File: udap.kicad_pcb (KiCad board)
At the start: 2 copper layers, 25 x 10 mm, 25 parts, among them J201 Conn_02x04_Counter_Clockwise, P1 USB_C_Plug, U2 MIC5245-3.3YM5, U201 NUF6401MNT1, U202 STM32F042F6Px, U4 NUF2042XV6T1G

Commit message: Minor fix
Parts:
- moved C2 0.40 mm to (93.5, 106.0)
- moved C5 0.40 mm to (94.6, 106.0)
- moved F1 0.14 mm to (95.9, 109.4)
- moved C1 0.10 mm to (105.5, 108.3)
- moved R2 0.10 mm to (105.5, 110.1)
- moved C3 0.10 mm to (96.2, 106.9)
- moved C4 0.10 mm to (105.5, 107.4)
- moved R201 0.10 mm to (105.5, 109.2)
- moved R202 0.10 mm to (105.5, 106.5)
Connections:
- net /bmp_core/BOOT0 renamed /core/BOOT0
- net /bmp_core/DM_P renamed /core/DM_P
- net /bmp_core/DP_P renamed /core/DP_P
- net /bmp_core/LED0 renamed /core/LED0
- net /bmp_core/LED1 renamed /core/LED1
- net /bmp_core/NRST renamed /core/NRST
- net /bmp_core/SWCLK renamed /core/SWCLK
- net /bmp_core/SWDIO renamed /core/SWDIO
- net /bmp_core/TGT_RST renamed /core/TGT_RST
- net /bmp_core/TGT_RX renamed /core/TGT_RX
- net /bmp_core/TGT_SWCLK renamed /core/TGT_SWCLK
- net /bmp_core/TGT_SWCLKo renamed /core/TGT_SWCLKo
- net /bmp_core/TGT_SWDIO renamed /core/TGT_SWDIO
- net /bmp_core/TGT_SWDIOo renamed /core/TGT_SWDIOo
- net /bmp_core/TGT_SWO renamed /core/TGT_SWO
- net /bmp_core/TGT_SWOo renamed /core/TGT_SWOo
- net /bmp_core/TGT_TX renamed /core/TGT_TX
- J201 pad 2: /bmp_core/TGT_RSTo -> /core/TGT_RXo
- J201 pad 3: /bmp_core/TGT_RXo -> /core/TGT_TXo
- J201 pad 4: /bmp_core/TGT_TXo -> GND
- J201 pad 8: GND -> /core/TGT_RSTo
- U201 pad 10: /bmp_core/TGT_RSTo -> /core/TGT_RSTo
- U201 pad 7: /bmp_core/TGT_RXo -> /core/TGT_RXo
- U201 pad 8: /bmp_core/TGT_TXo -> /core/TGT_TXo
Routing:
- net /bmp_core/TGT_RSTo: track 7.58 -> 0.00 mm, vias 2 -> 0
- net /core/TGT_RSTo: track 0.00 -> 7.10 mm, vias 0 -> 1
- net /bmp_core/TGT_TXo: track 6.34 -> 0.00 mm
- net /core/TGT_RXo: track 0.00 -> 6.11 mm
- net /bmp_core/TGT_RXo: track 5.49 -> 0.00 mm
- net /core/TGT_TXo: track 0.00 -> 5.28 mm
- net +3V3: track 21.8 -> 18.2 mm, vias 3 -> 1
- net /core/BOOT0: track 3.45 -> 4.27 mm
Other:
- board text added: "G"

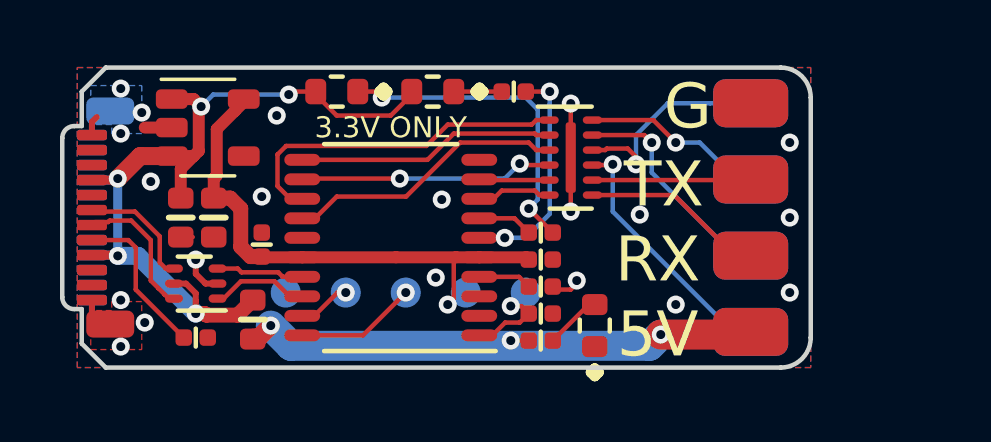
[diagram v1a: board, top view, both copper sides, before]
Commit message: Rotate D2 to move its silk screen in-bounds
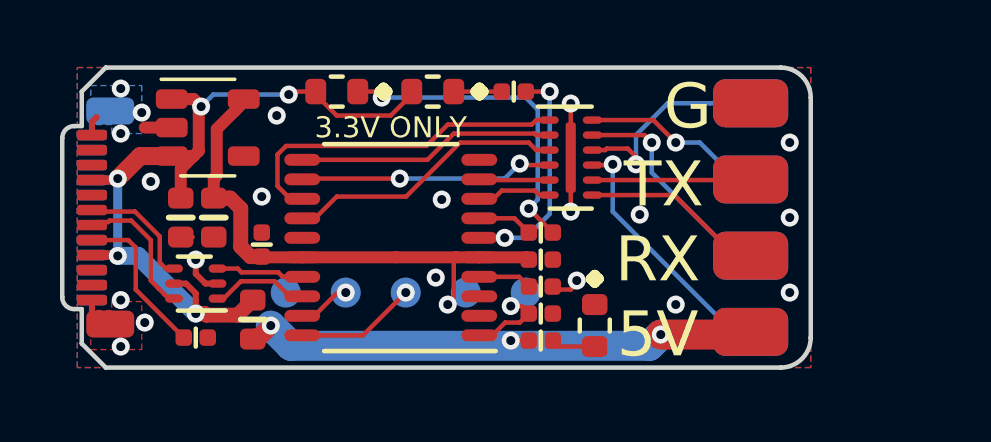
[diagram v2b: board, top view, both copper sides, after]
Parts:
- turned D2 to 270 degrees
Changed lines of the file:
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@@
     (thickness 0.7)
     (drawings 30)
-    (tracks 261)
+    (tracks 262)
     (zones 0)
     (modules 25)
@@
   )
   (module leds:LEDC1608X60 (layer F.Cu)
-    (at 107.3 109.6 90)
+    (at 107.3 109.6 270)
     (descr "LED,Chip;1.60mm L X 0.80mm W X 0.60mm H")
     (attr smd)
@@
       (effects (font (size 0.4 0.4) (thickness 0.075)))
     )
-    (pad 2 smd roundrect (at 0.7 0 90) (size 0.7 0.85) (layers F.Cu F.Paste F.Mask) (roundrect_rratio 0.25)
+    (pad 2 smd roundrect (at 0.7 0 270) (size 0.7 0.85) (layers F.Cu F.Paste F.Mask) (roundrect_rratio 0.25)
       (net 14 "Net-(D2-Pad2)"))
-    (pad 1 smd roundrect (at -0.7 0 90) (size 0.7 0.85) (layers F.Cu F.Paste F.Mask) (roundrect_rratio 0.25)
+    (pad 1 smd roundrect (at -0.7 0 270) (size 0.7 0.85) (layers F.Cu F.Paste F.Mask) (roundrect_rratio 0.25)
       (net 2 GND))
     (model ${KIPRJMOD}/kicad_libs/3dmodels/step/LED_0603_G.STEP
@@
   (segment (start 104.775 107.975) (end 105.1 108.3) (width 0.15) (layer F.Cu) (net 13))
   (segment (start 103.45 107.975) (end 104.775 107.975) (width 0.15) (layer F.Cu) (net 13))
-  (segment (start 107.1 108.9) (end 107.3 108.9) (width 0.15) (layer F.Cu) (net 14))
-  (segment (start 105.9 110.1) (end 107.1 108.9) (width 0.15) (layer F.Cu) (net 14))
+  (segment (start 107.1 108.9) (end 107.3 108.9) (width 0.15) (layer F.Cu) (net 2))
+  (segment (start 106.1 110.3) (end 105.9 110.1) (width 0.15) (layer F.Cu) (net 14))
+  (segment (start 107.3 110.3) (end 106.1 110.3) (width 0.15) (layer F.Cu) (net 14))
   (segment (start 92 107) (end 92 108.4) (width 0.15) (layer F.Cu) (net 15))
   (segment (start 90.54 106.75) (end 91.75 106.75) (width 0.15) (layer F.Cu) (net 15))
